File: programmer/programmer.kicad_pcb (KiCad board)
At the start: 2 copper layers, 55.4 x 38.1 mm, 15 parts, among them J1 USB_A, J2 PWR, J3 PICKIT, J4 POGO_BOARD, J5 TEST_2P

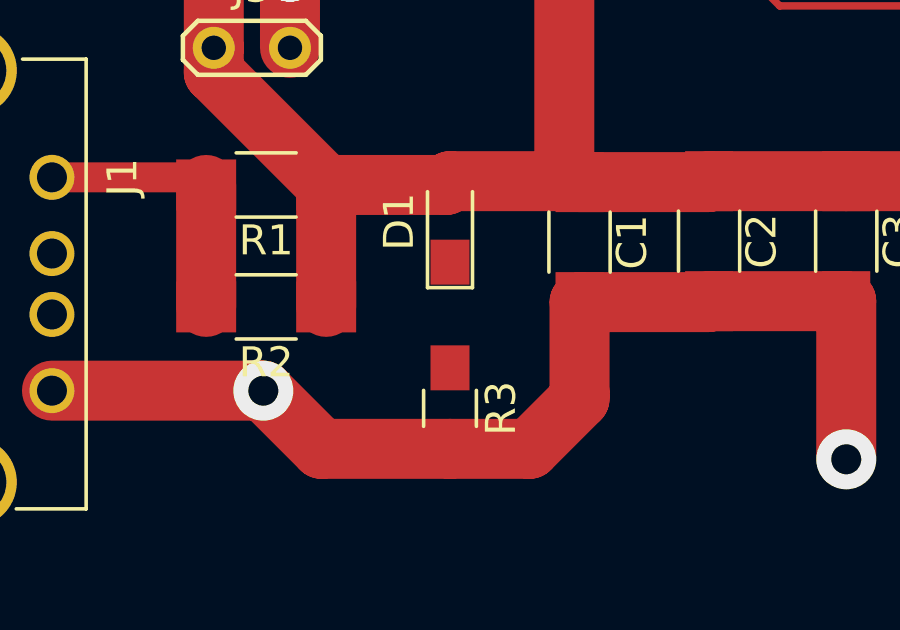
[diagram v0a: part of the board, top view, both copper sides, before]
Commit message: Fix missing trace.
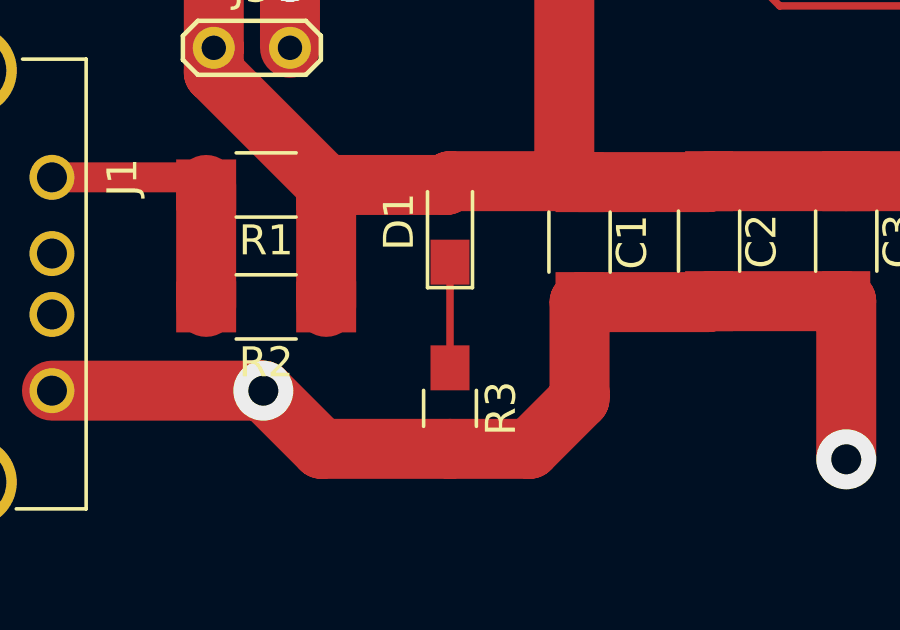
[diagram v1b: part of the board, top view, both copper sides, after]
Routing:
- net Net-(D1-Pad1): track 0.00 -> 3.52 mm
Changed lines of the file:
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@@
 (kicad_pcb (version 4) (host pcbnew 4.0.6+dfsg1-1)
   (general
-    (links 0)
-    (no_connects 24)
+    (links 24)
+    (no_connects 2)
     (area 124.384999 89.840999 179.907001 128.091001)
     (thickness 1.6)
     (drawings 6)
-    (tracks 64)
+    (tracks 65)
     (zones 0)
     (modules 15)
@@
   )
   (setup
-    (last_trace_width 2)
+    (last_trace_width 0.25)
     (user_trace_width 0.25)
     (user_trace_width 1)
@@
       (net 2 GND))
     (model ${KISYS3DMOD}/Pin_Headers.3dshapes/Pin_Header_Angled_1x02_Pitch2.54mm.wrl
-      (at (xyz 0 0 0))
-      (scale (xyz 1 1 1))
-      (rotate (xyz 0 0 0))
+      (at (xyz 0 -0.05 0))
+      (scale (xyz 1 1 1))
+      (rotate (xyz 0 0 90))
     )
   )
@@
       (net 11 "Net-(J3-Pad6)"))
     (model ${KISYS3DMOD}/Pin_Headers.3dshapes/Pin_Header_Angled_1x06_Pitch2.54mm.wrl
-      (at (xyz 0 0 0))
-      (scale (xyz 1 1 1))
-      (rotate (xyz 0 0 0))
+      (at (xyz 0 -0.25 0))
+      (scale (xyz 1 1 1))
+      (rotate (xyz 0 0 90))
     )
   )
@@
   (segment (start 171.3484 109.1184) (end 171.323 109.093) (width 2) (layer F.Cu) (net 2))
   (via (at 171.323 109.093) (size 2) (drill 1) (layers F.Cu B.Cu) (net 2))
+  (segment (start 144.526 109.888) (end 144.526 113.411) (width 0.25) (layer F.Cu) (net 3))
   (segment (start 131.2575 107.061) (end 136.144 107.061) (width 1) (layer F.Cu) (net 6))
   (segment (start 136.144 107.061) (end 136.398 107.315) (width 1) (layer F.Cu) (net 6))

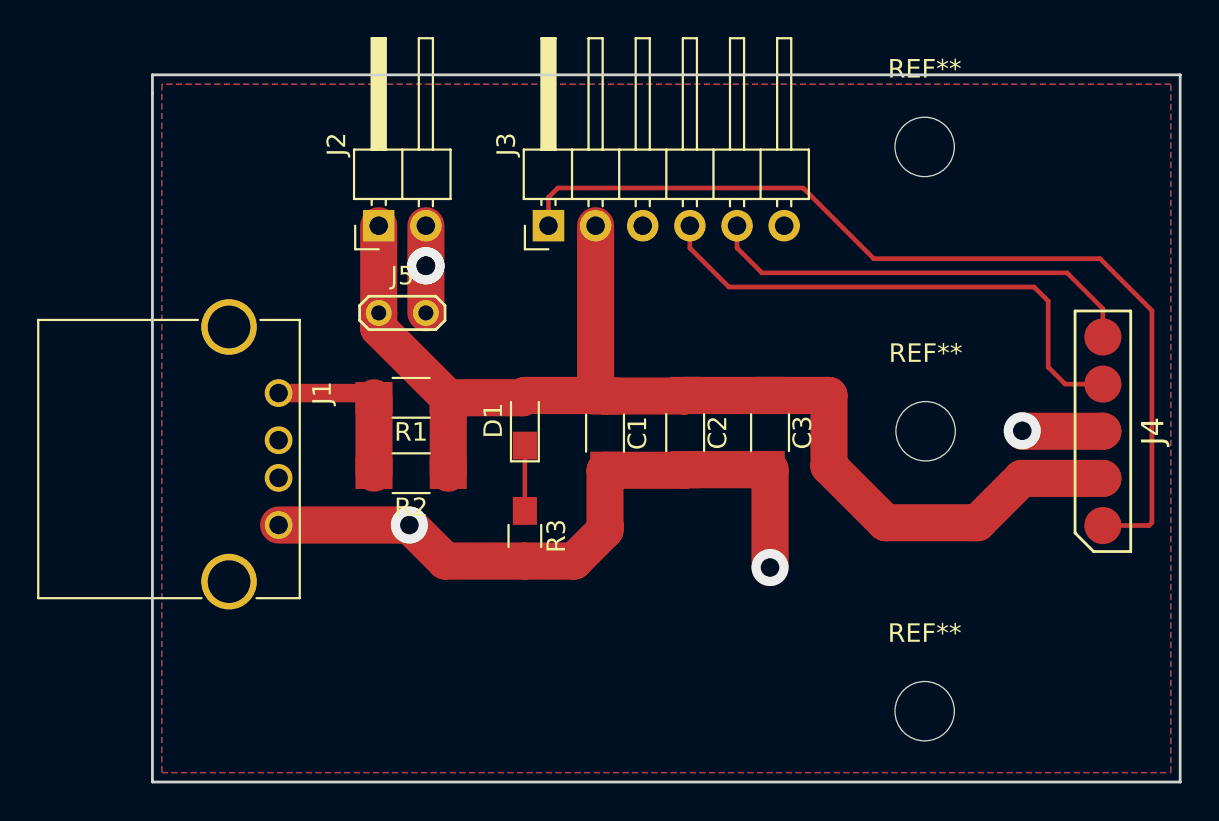
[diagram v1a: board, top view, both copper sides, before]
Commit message: Update programmer
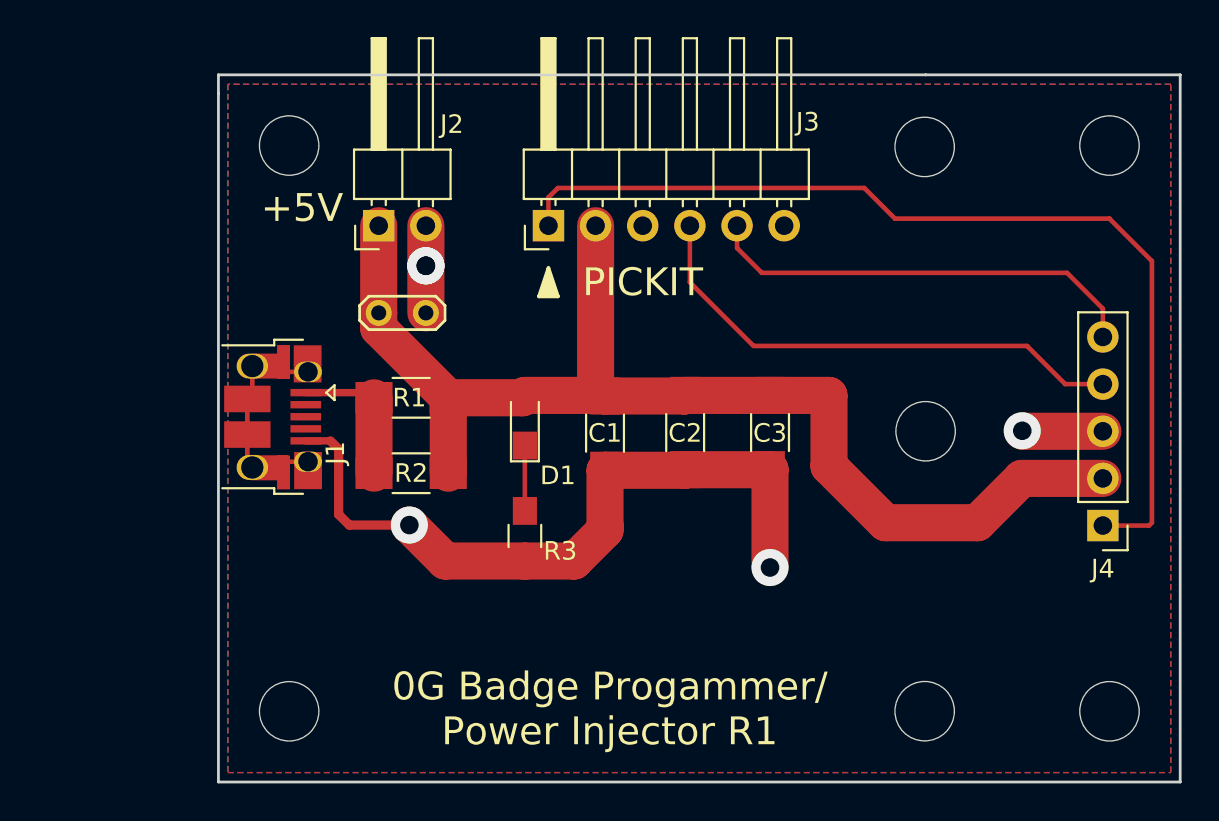
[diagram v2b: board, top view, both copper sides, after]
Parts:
- added REF**: MountingHole_3.2mm_M3, Mounting_Holes:MountingHole_3.2mm_M3, F.Cu at (176.0, 93.7)
- added REF**: MountingHole_3.2mm_M3, Mounting_Holes:MountingHole_3.2mm_M3, F.Cu at (176.0, 124.2)
- added REF**: MountingHole_3.2mm_M3, Mounting_Holes:MountingHole_3.2mm_M3, F.Cu at (131.8, 124.2)
- added REF**: MountingHole_3.2mm_M3, Mounting_Holes:MountingHole_3.2mm_M3, F.Cu at (131.8, 93.7)
- J1: value USB_A -> USB_OTG; footprint Connect:USB_A -> prog:USB_Micro-B_Amphenol_10103594-0001LF_Horizontal-circ
- J4: footprint prog:SMD-5 -> Pin_Headers:Pin_Header_Straight_1x05_Pitch2.54mm
- moved J4 5.08 mm to (175.7, 114.2), turned to 180 degrees
- moved J1 1.34 mm to (131.0, 108.4)
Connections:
- J1 pad 4: GND -> Net-(J1-Pad4)
- J1 pad 5: Net-(J1-Pad5) -> GND
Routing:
- net Net-(J1-Pad6): track 0.00 -> 11.9 mm
- net GND: track 45.5 -> 48.0 mm
- net /~MCLR: track 51.1 -> 52.7 mm
- net Net-(J1-Pad1): track 9.31 -> 8.21 mm
- net /PGD: track 28.6 -> 27.6 mm
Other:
- board size 55.4 x 38.1 mm -> 51.8 x 38.1 mm
- board text added: "+5V"
- board text added: "0G Badge Progammer/ Power Injector R1"
- board text added: "PICKIT"
